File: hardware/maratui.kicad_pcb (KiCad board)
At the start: 2 copper layers, 69 x 49.5 mm, 6 parts, among them J1 Left, J2 Button, J3 Rigt, J4 Mara, J5 TFT

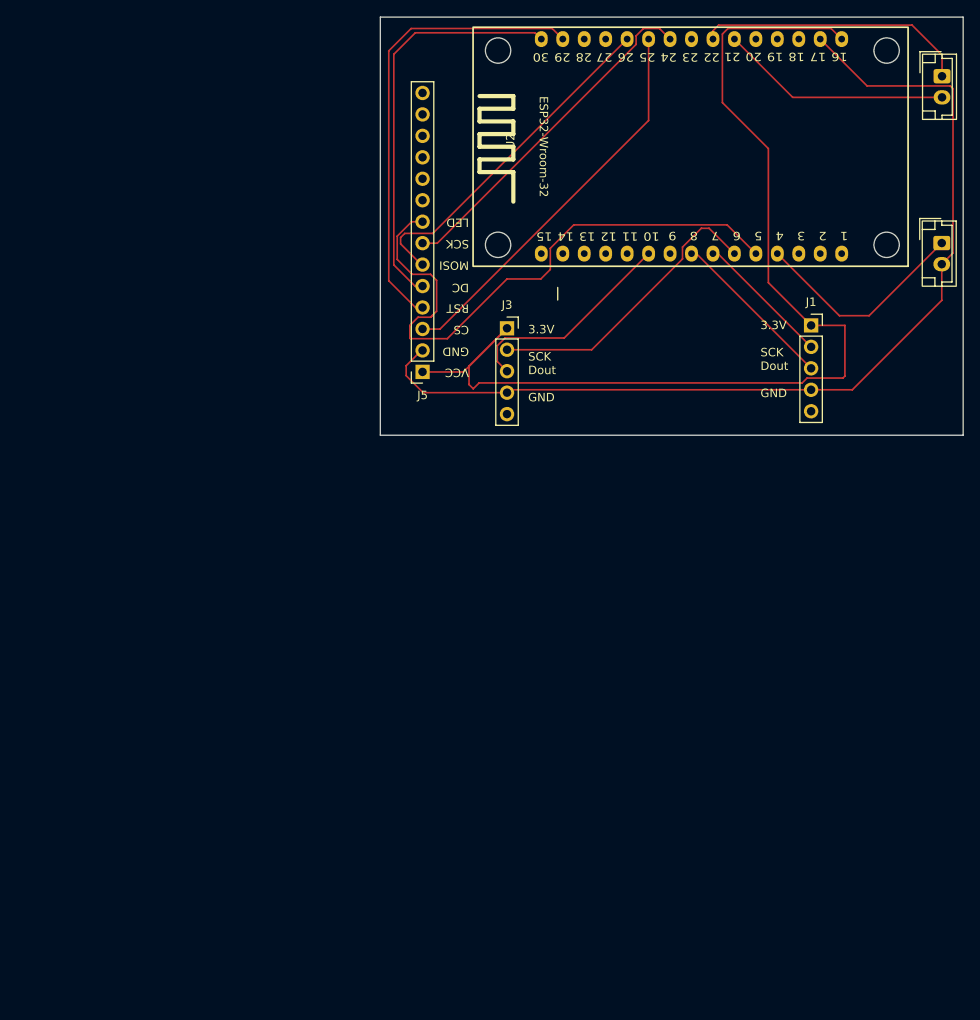
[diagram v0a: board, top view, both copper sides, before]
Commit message: feat(hardware): rework schematic/PCB and reorganize KiCad library
Consolidates the ESP32, HX711 and TFT footprints/symbols/3D models into
a single hardware/lib/ tree (3dshapes, footprints.pretty, symbols),
replacing the old per-part library layout. Adds a BOM export (maratui.csv).

Co-Authored-By: Claude Sonnet 5 <noreply@anthropic.com>
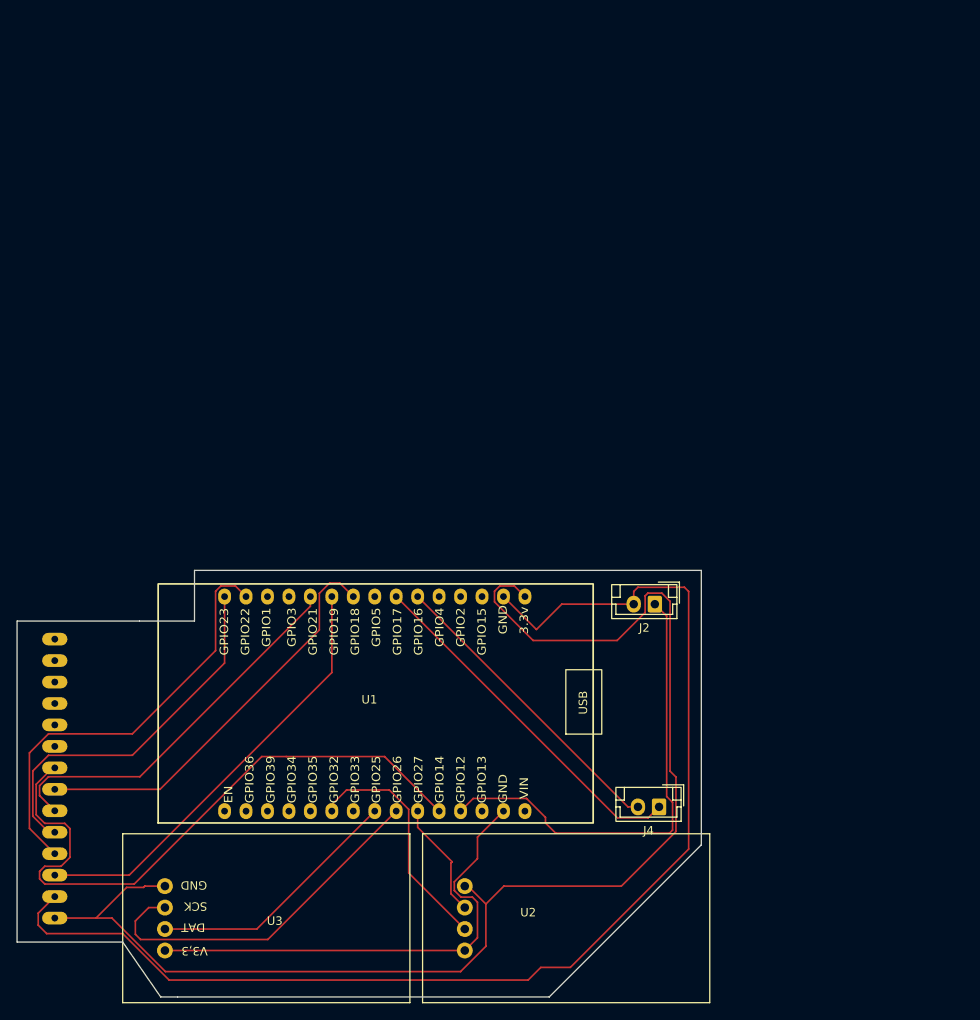
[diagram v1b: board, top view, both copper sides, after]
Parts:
- removed J1: Left, Connector_PinSocket_2.54mm:PinSocket_1x05_P2.54mm_Vertical
- removed J3: Rigt, Connector_PinSocket_2.54mm:PinSocket_1x05_P2.54mm_Vertical
- removed J5: TFT, Connector_PinSocket_2.54mm:PinSocket_1x14_P2.54mm_Vertical
- added U1: ~, waage:ESP32_30pin, F.Cu at (84.6, 132.6)
- added U3: HX711, waage:HX711_module, F.Cu at (71.0, 157.2)
- added U4: TFT_320x240, waage:TFT-320x240, B.Cu at (46.0, 140.7)
- J4: value Mara -> Conn_01x02_Socket
- U2: value ~ -> HX711; footprint Maratui Footprints:ESP32_30pin -> waage:HX711_module
- moved J4 92.8 mm to (117.5, 144.0), turned to 180 degrees
- moved U2 92.4 mm to (106.5, 157.2)
- moved J2 54.6 mm to (117.0, 120.0), turned to 180 degrees
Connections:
- J2 pad 1: /BUTTON -> Net-(J2-Pin_1)
- J2 pad 2: GND -> Net-(J2-Pin_2)
- U2 pad 10: Dat_32 -> Net-(U2-GND)
- U2 pad 7: SCK_26 -> Net-(U1-3.3v)
- U2 pad 8: Dat_25 -> SCK_27
- U2 pad 9: unconnected-(U2-GPIO33-Pad9) -> Dat_32
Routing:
- net Net-(U1-3.3v): track 0.00 -> 158.4 mm
- net Net-(J2-Pin_2): track 0.00 -> 147.5 mm
- net +3.3V: track 130.4 -> 0.00 mm
- net GND: track 116.3 -> 0.00 mm
- net LED_14: track 0.00 -> 76.3 mm
- net /LED: track 70.9 -> 0.00 mm
- net Net-(U2-GND): track 0.00 -> 57.0 mm
- net Net-(J2-Pin_1): track 0.00 -> 55.6 mm
- net SCK_26: track 16.2 -> 43.2 mm
- net /BUTTON: track 26.1 -> 0.00 mm
- net SCK_27: track 34.9 -> 13.8 mm
- net Dat_25: track 19.8 -> 30.6 mm
- net Net-(J4-Pin_1): track 32.3 -> 42.5 mm
- net Net-(J4-Pin_2): track 27.4 -> 36.4 mm
- net sck_18: track 41.1 -> 48.7 mm
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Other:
- board size 69 x 49.5 mm -> 81 x 50.5 mm
- board text removed: "3.3V SCK Dout GND"
- board text removed: "CS"
- board text removed: "DC"
- board text removed: "ESP32-Wroom-32"
- board text removed: "GND"
- board text removed: "LED"
- board text removed: "MOSI"
- board text removed: "RST"
- board text removed: "SCK"
- board text removed: "VCC"
